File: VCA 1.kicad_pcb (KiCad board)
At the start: 2 copper layers, 171.3 x 128.5 mm, 89 parts, among them J1 Eurorack 2x8hs, J10 CV2, J11 IN2, J12 IN 1x8h, J13 OUT1, J14 OUT2, J15 IN 1x8s, J2 OUT 1x3s, J3 CV 1x9s, J5 CV 1x9h, J6 OUT 1x3h, J8 CV1, J9 IN1, Q1 2N3904, Q2 2N3904, U1 TL074, U2 AS2164

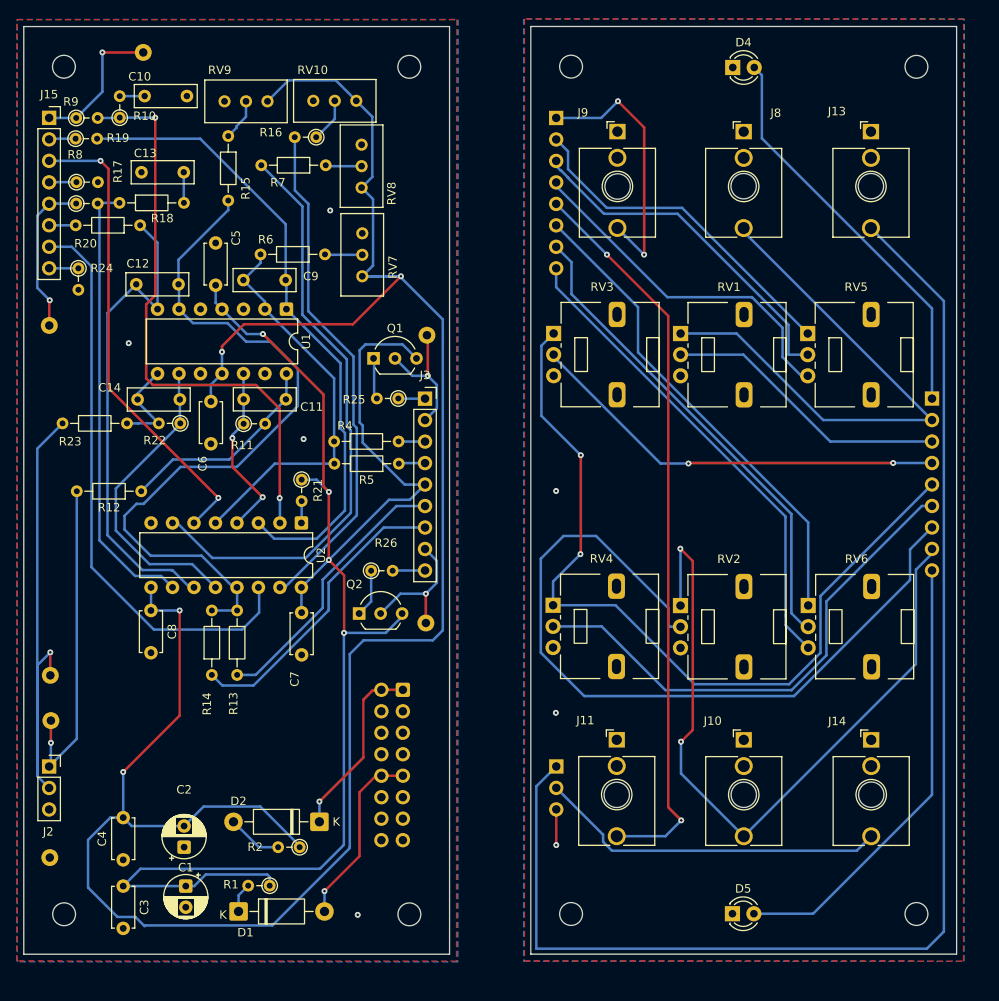
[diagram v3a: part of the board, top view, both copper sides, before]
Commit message: Updated to use CNC constraints
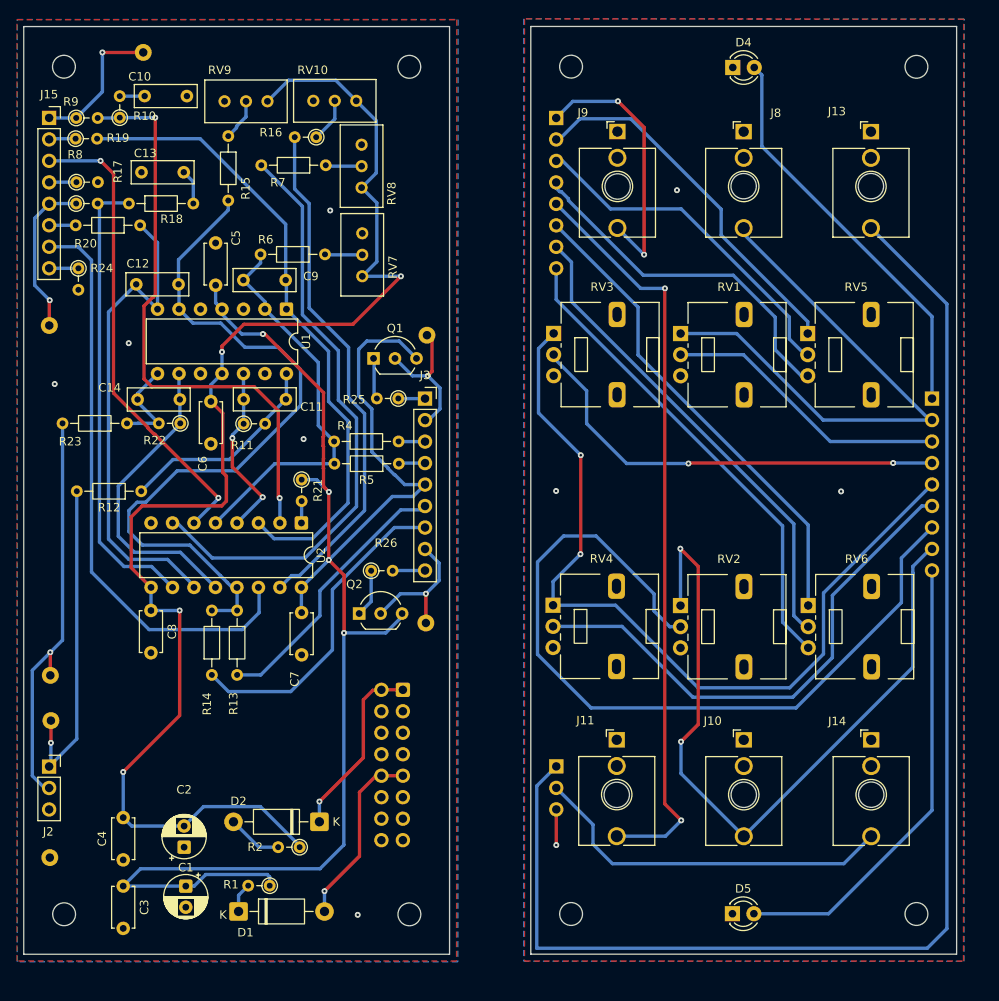
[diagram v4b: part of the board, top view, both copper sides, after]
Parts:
- moved R18 1.11 mm to (37.4, 50.9)
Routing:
- net -12V: track 282.4 -> 186.0 mm
- net Net-(J2-Pin_2): track 62.9 -> 48.5 mm
- net Net-(J12-Pin_2): track 40.5 -> 43.9 mm
- net Net-(J3-Pin_7): track 35.4 -> 38.2 mm
- net Net-(J5-Pin_7): track 93.1 -> 95.9 mm
- net Net-(J5-Pin_4): track 50.2 -> 52.6 mm
- net Net-(J6-Pin_2): track 41.5 -> 43.7 mm
- net Net-(J12-Pin_5): track 87.4 -> 89.1 mm
- net Net-(J5-Pin_6): track 60.7 -> 62.0 mm
- net Net-(U2-I_IN3): track 53.5 -> 54.7 mm
- net +12V: track 205.2 -> 206.3 mm
- net Net-(D5-A): track 53.4 -> 54.5 mm
- net Net-(U2-I_IN4): track 60.4 -> 61.4 mm
- net Net-(J3-Pin_2): track 16.3 -> 17.3 mm
- net Net-(J12-Pin_3): track 41.7 -> 40.8 mm
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
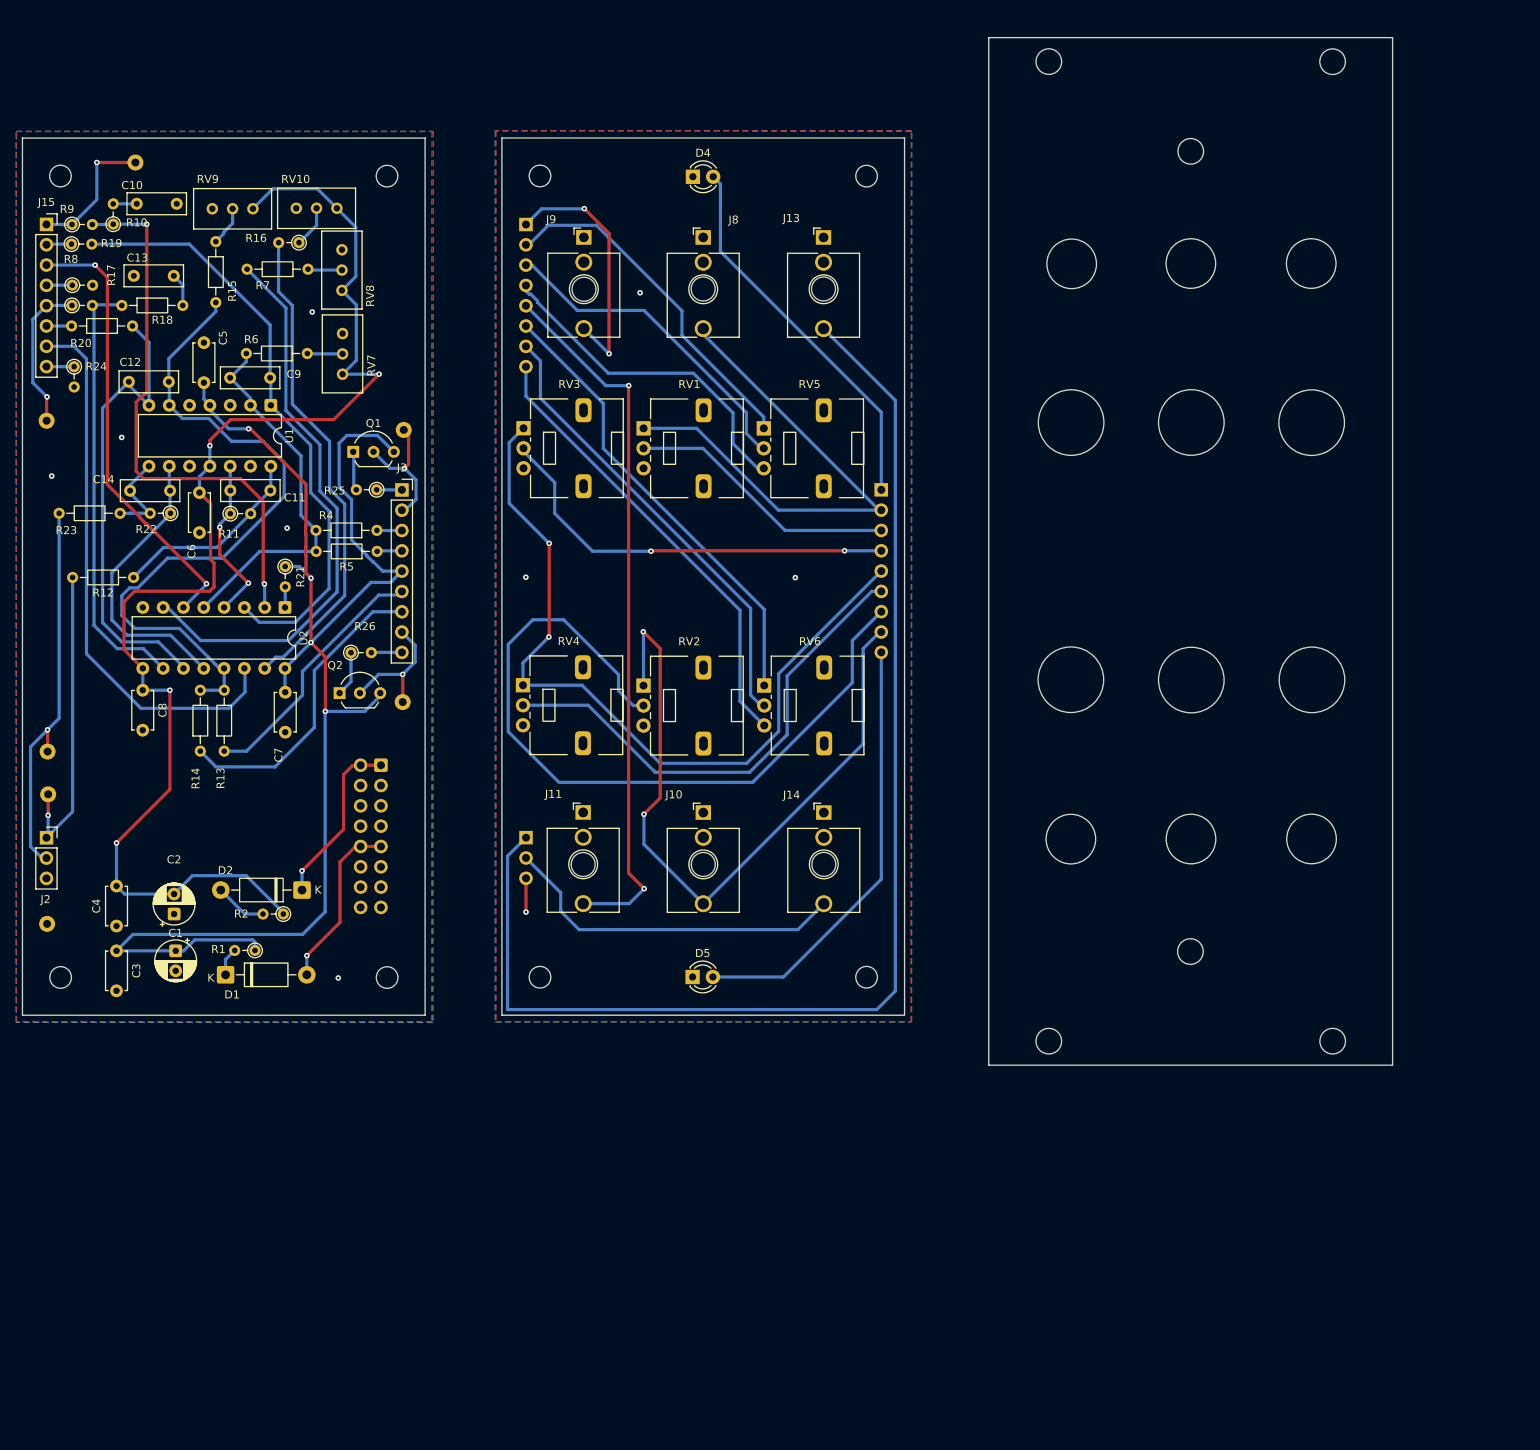
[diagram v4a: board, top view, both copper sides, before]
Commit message: Rotated PCB for CNC use
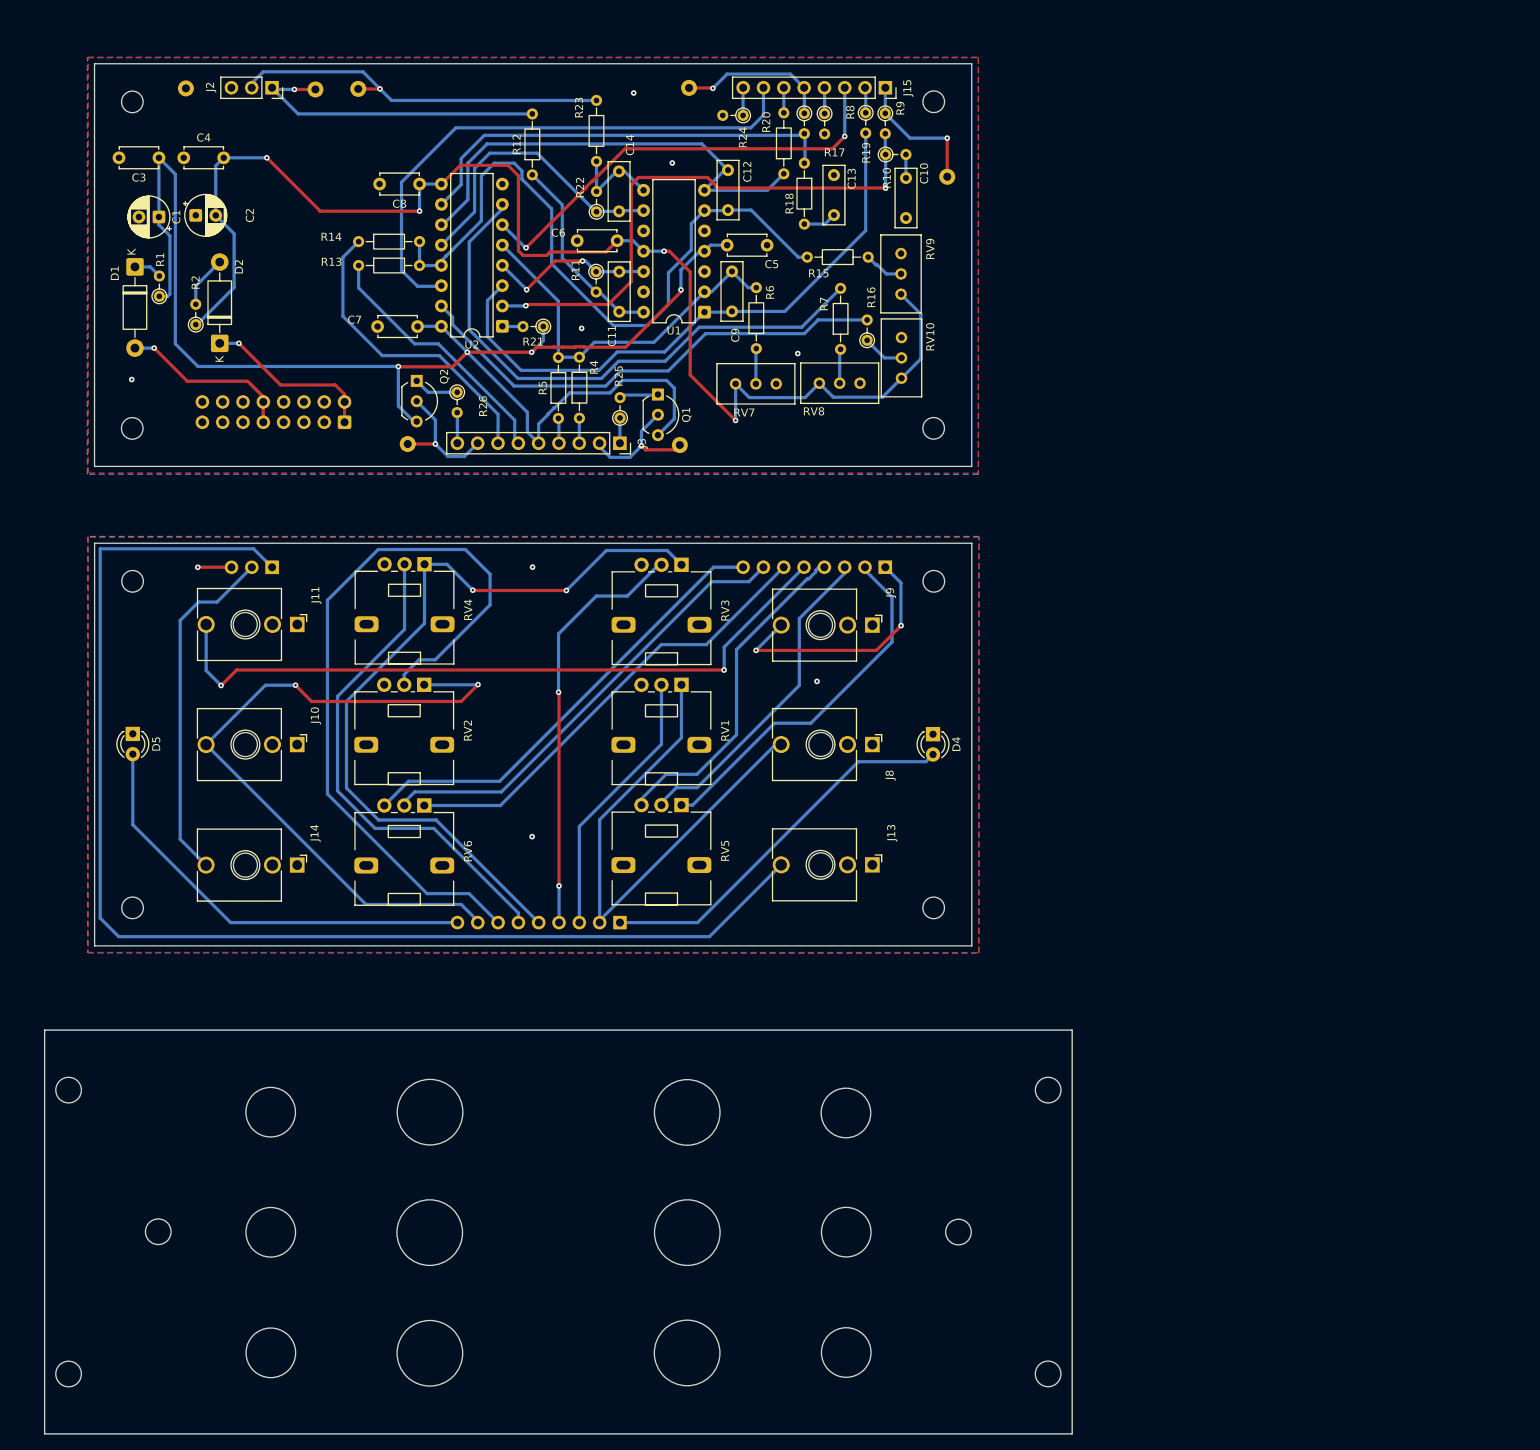
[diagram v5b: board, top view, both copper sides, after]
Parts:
- moved H10 167.9 mm to (153.3, 184.5), turned to -90 degrees
- moved H11 163.5 mm to (30.8, 184.5), turned to -90 degrees
- moved H9 128.6 mm to (153.3, 149.0), turned to -90 degrees
- moved H12 122.7 mm to (30.8, 149.0), turned to -90 degrees
- moved H3 109.9 mm to (38.7, 25.4), turned to -90 degrees
- moved H1 109.6 mm to (139.0, 25.4), turned to -90 degrees
- moved J15 106.3 mm to (132.9, 23.6), turned to -90 degrees
- moved TP1 105.9 mm to (45.4, 23.7), turned to -90 degrees
- moved R9 102.6 mm to (132.9, 26.8), turned to -90 degrees
- moved TP4 101.5 mm to (140.7, 34.8), turned to 90 degrees
- moved R19 100.7 mm to (130.4, 26.8), turned to -90 degrees
- moved C3 99.3 mm to (42.1, 32.4), turned to 180 degrees
- moved J2 97.9 mm to (56.2, 23.6), turned to -90 degrees
- moved R10 97.0 mm to (132.9, 32.0), turned to 0 degrees
- moved R8 96.5 mm to (125.3, 26.9), turned to -90 degrees
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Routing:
- net Net-(J12-Pin_2): track 43.9 -> 45.5 mm
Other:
- board size 171.3 x 128.5 mm -> 128.5 x 171.3 mm
